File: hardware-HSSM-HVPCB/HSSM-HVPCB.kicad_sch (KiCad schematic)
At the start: 72 parts, among them J2 2601-1110, J3 Connector_BTB_20021311-00010T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, K1 G6DN-1A-L DC12, K2 G6DN-1A-L DC12, Q1 Q_NMOS_SOT-23_IRLML6344, Q2 Q_NMOS_SOT-23_IRLML6344, U1 LNK3204D-TL, U2 CS5480-INZ, U3 LTV-354T, U4 LTV-354T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

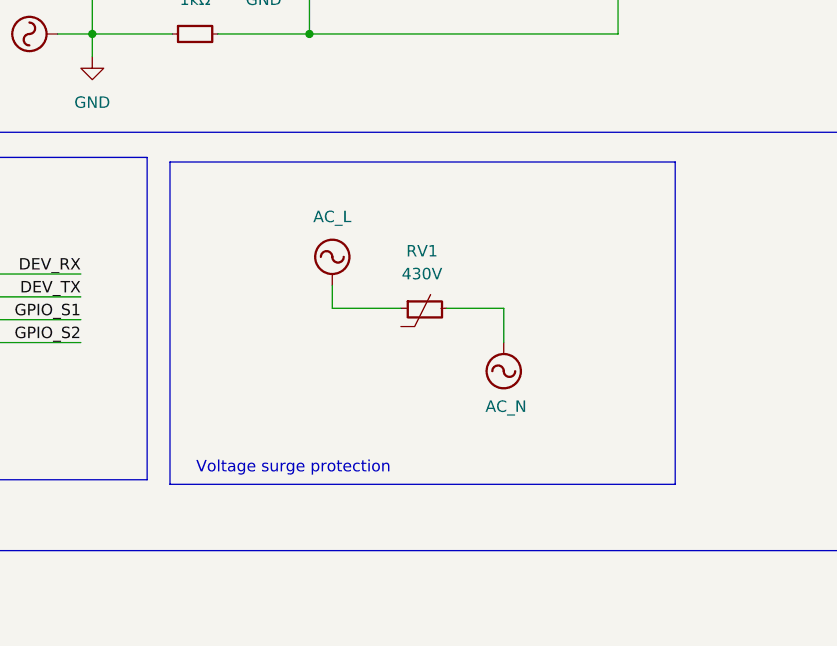
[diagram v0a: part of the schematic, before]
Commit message: [#6] Remove surge protection
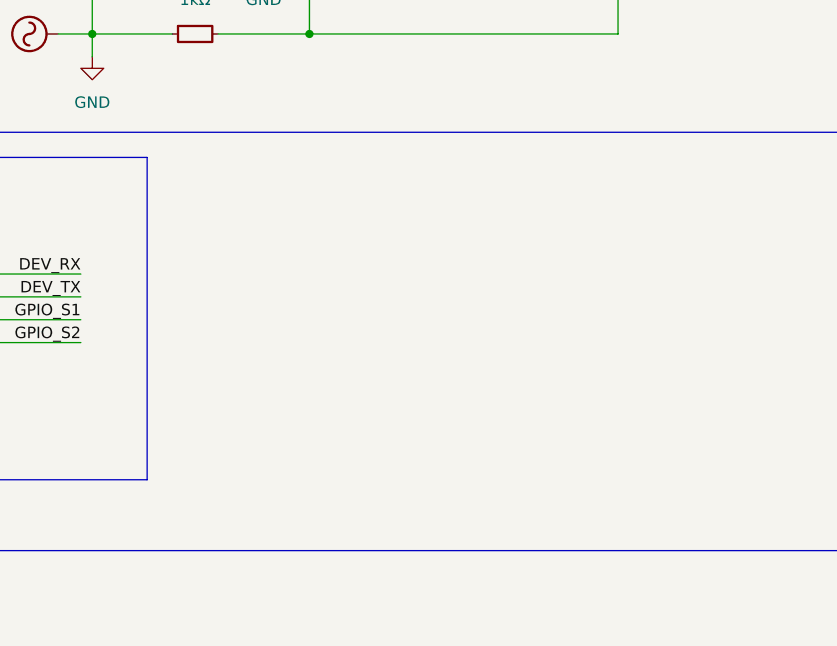
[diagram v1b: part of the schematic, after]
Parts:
- removed RV1: Varistor_MOV-14D431K, HSSM-HVPCB:MOV-14D431K, symbol HSSM-HVPCB:Varistor_MOV-14D431K
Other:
- note removed: "Voltage surge protection"

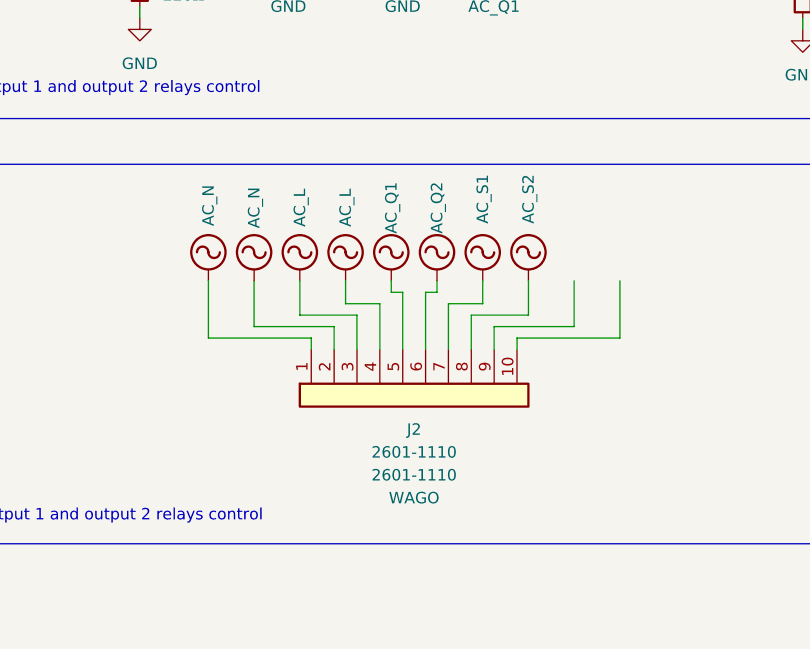
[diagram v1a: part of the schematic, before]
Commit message: [#6] Replace wago terminal with 8 pos variant
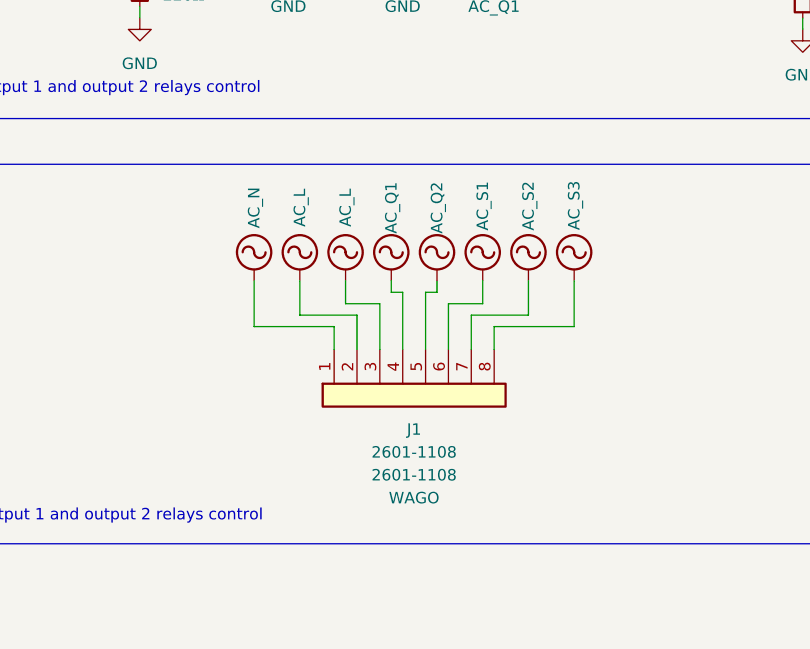
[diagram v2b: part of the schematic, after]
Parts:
- removed J2: 2601-1110, HSSM-HVPCB:2601-1110, symbol HSSM-HVPCB:terminal_1x10_2601-1110_wago
- added J1: 2601-1108, HSSM-HVPCB:2601-1108, symbol HSSM-HVPCB:terminal_1x8_2601-1108_wago
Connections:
- net AC_L: now also J1.2 (Pin_2), J1.3 (Pin_3)
- net AC_N: now also J1.1 (Pin_1)
- net AC_Q1: now also J1.4 (Pin_4)
- net AC_Q2: now also J1.5 (Pin_5)
- net AC_S1: now also J1.6 (Pin_6)
- net AC_S2: now also J1.7 (Pin_7)
- new net AC_S3: J1.8 (Pin_8)
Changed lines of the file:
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@@
 	(wire
 		(pts
-			(xy 278.13 229.87) (xy 278.13 228.6)
-		)
-		(stroke
-			(width 0)
-			(type default)
-		)
-	)
-	(wire
-		(pts
 			(xy 381 63.5) (xy 381 71.12)
 		)
@@
 	(wire
 		(pts
-			(xy 300.99 229.87) (xy 300.99 228.6)
-		)
-		(stroke
-			(width 0)
-			(type default)
-		)
-	)
-	(wire
-		(pts
 			(xy 386.08 71.12) (xy 386.08 73.66)
 		)
@@
 	(wire
 		(pts
-			(xy 266.7 228.6) (xy 266.7 222.25)
-		)
-		(stroke
-			(width 0)
-			(type default)
-		)
-	)
-	(wire
-		(pts
 			(xy 289.56 59.69) (xy 294.64 59.69)
 		)
@@
 	(wire
 		(pts
-			(xy 278.13 228.6) (xy 266.7 228.6)
-		)
-		(stroke
-			(width 0)
-			(type default)
-		)
-	)
-	(wire
-		(pts
 			(xy 354.33 46.99) (xy 354.33 52.07)
 		)
@@
 	(wire
 		(pts
-			(xy 312.42 228.6) (xy 312.42 222.25)
-		)
-		(stroke
-			(width 0)
-			(type default)
-		)
-	)
-	(wire
-		(pts
-			(xy 300.99 228.6) (xy 312.42 228.6)
-		)
-		(stroke
-			(width 0)
-			(type default)
-		)
-	)
-	(wire
-		(pts
 			(xy 350.52 185.42) (xy 350.52 187.96)
 		)
@@
 	)
 	(symbol
+		(lib_id "power:AC")
+		(at 307.34 222.25 0)
+		(unit 1)
+		(exclude_from_sim no)
+		(in_bom yes)
+		(on_board yes)
+		(dnp no)
+		(property "Reference" "#PWR030"
+			(at 307.34 224.79 0)
+			(effects
+				(font
+					(size 1.27 1.27)
+				)
+				(hide yes)
+			)
+		)
+		(property "Value" "AC_S3"
+			(at 307.34 213.868 90)
+			(effects
+				(font
+					(size 1.27 1.27)
+				)
+			)
+		)
+		(property "Footprint" ""
+			(at 307.34 222.25 0)
+			(effects
+				(font
+					(size 1.27 1.27)
+				)
+				(hide yes)
+			)
+		)
+		(property "Datasheet" ""
+			(at 307.34 222.25 0)
+			(effects
+				(font
+					(size 1.27 1.27)
+				)
+				(hide yes)
+			)
+		)
+		(property "Description" "Power symbol creates a global label with name \"AC\""
+			(at 307.34 222.25 0)
+			(effects
+				(font
+					(size 1.27 1.27)
+				)
+				(hide yes)
+			)
+		)
+		(pin "1"
+		)
+		(instances
+			(project "HSSM-HVPCB"
+				(path "/e1056638-7c6b-48e4-9e2e-c0f7b783eee5"
+					(reference "#PWR030")
+					(unit 1)
+				)
+			)
+		)
+	)
+	(symbol
 		(lib_id "HSSM-HVPCB:TPS560200DBVR_SOIC_6_TI")
 		(at 124.46 237.49 180)
@@
 	)
 	(symbol
-		(lib_id "power:AC")
-		(at 101.6 64.77 0)
-		(unit 1)
-		(exclude_from_sim no)
-		(in_bom yes)
-		(on_board yes)
-		(dnp no)
-		(property "Reference" "#PWR041"
-			(at 101.6 67.31 0)
-			(effects
-				(font
-					(size 1.27 1.27)
-				)
-				(hide yes)
-			)
-		)
-		(property "Value" "AC_L"
-			(at 101.6 58.166 0)
-			(effects
-				(font
-					(size 1.27 1.27)
-				)
-			)
-		)
-		(property "Footprint" ""
-			(at 101.6 64.77 0)
-			(effects
-				(font
-					(size 1.27 1.27)
-				)
-				(hide yes)
-			)
-		)
-		(property "Datasheet" ""
-			(at 101.6 64.77 0)
-			(effects
-				(font
-					(size 1.27 1.27)
-				)
-				(hide yes)
-			)
-		)
-		(property "Description" "Power symbol creates a global label with name \"AC\""
-			(at 101.6 64.77 0)
-			(effects
-				(font
-					(size 1.27 1.27)
-				)
-				(hide yes)
-			)
-		)
-		(pin "1"
-		)
-		(instances
-			(project "HSSM-HVPCB"
-				(path "/e1056638-7c6b-48e4-9e2e-c0f7b783eee5"
-					(reference "#PWR041")
-					(unit 1)
-				)
-			)
-		)
-	)
-	(symbol
-		(lib_id "HSSM-HVPCB:terminal_1x10_2601-1110_wago")
-		(at 288.29 234.95 90)
+		(lib_id "HSSM-HVPCB:terminal_1x8_2601-1108_wago")
+		(at 289.56 234.95 90)
 		(mirror x)
 		(unit 1)
@@
 		(on_board yes)
 		(dnp no)
-		(property "Reference" "J2"
+		(property "Reference" "J1"
 			(at 289.56 238.76 90)
 			(effects
@@
 			)
 		)
-		(property "Value" "2601-1110"
+		(property "Value" "2601-1108"
 			(at 289.56 241.3 90)
 			(effects
@@
 			)
 		)
-		(property "Footprint" "HSSM-HVPCB:2601-1110"
-			(at 288.29 234.95 0)
+		(property "Footprint" "HSSM-HVPCB:2601-1108"
+			(at 290.83 234.95 0)
 			(effects
 				(font
@@
 			)
 		)
-		(property "Datasheet" "https://www.farnell.com/datasheets/3775116.pdf"
-			(at 288.29 234.95 0)
+		(property "Datasheet" "https://source.z2data.com/2022/11/30/3/26/12/266816/8679706/WAGO26011108enUS.pdf"
+			(at 290.83 234.95 0)
 			(effects
 				(font
@@
 			)
 		)
-		(property "Description" "terminal_1x10_2601-1110_wago"
-			(at 288.29 234.95 0)
+		(property "Description" "terminal_1x10_2601-1108_wago"
+			(at 290.83 234.95 0)
 			(effects
 				(font
@@
 			)
 		)
-		(property "MPN" "2601-1110"
+		(property "MPN" "2601-1108"
 			(at 289.56 243.84 90)
 			(effects
@@
 			)
 		)
-		(pin "10"
+		(pin "3"
 		)
 		(pin "2"
 		)
-		(pin "3"
-		)
 		(pin "1"
 		)
+		(pin "7"
+		)
 		(pin "4"
 		)
@@
 		(pin "6"
 		)
-		(pin "7"
-		)
 		(pin "8"
 		)
-		(pin "9"
-		)
 		(instances
-			(project "HSSM-HVPCB"
+			(project ""
 				(path "/e1056638-7c6b-48e4-9e2e-c0f7b783eee5"
-					(reference "J2")
+					(reference "J1")
 					(unit 1)
 				)
@@
 	(symbol
 		(lib_id "power:AC")
-		(at 266.7 222.25 0)
+		(at 101.6 64.77 0)
 		(unit 1)
 		(exclude_from_sim no)
@@
 		(on_board yes)
 		(dnp no)
-		(property "Reference" "#PWR040"
-			(at 266.7 224.79 0)
+		(property "Reference" "#PWR041"
+			(at 101.6 67.31 0)
 			(effects
 				(font
@@
 			)
 		)
-		(property "Value" "AC_N"
-			(at 266.7 213.868 90)
+		(property "Value" "AC_L"
+			(at 101.6 58.166 0)
 			(effects
 				(font
@@
 		)
 		(property "Footprint" ""
-			(at 266.7 222.25 0)
+			(at 101.6 64.77 0)
 			(effects
 				(font
@@
 		)
 		(property "Datasheet" ""
-			(at 266.7 222.25 0)
+			(at 101.6 64.77 0)
 			(effects
 				(font
@@
 		)
 		(property "Description" "Power symbol creates a global label with name \"AC\""
-			(at 266.7 222.25 0)
+			(at 101.6 64.77 0)
 			(effects
 				(font
@@
 			(project "HSSM-HVPCB"
 				(path "/e1056638-7c6b-48e4-9e2e-c0f7b783eee5"
-					(reference "#PWR040")
+					(reference "#PWR041")
 					(unit 1)
 				)
@@
 		(on_board yes)
 		(dnp no)
-		(fields_autoplaced yes)
 		(property "Reference" "#PWR029"
 			(at 302.26 224.79 0)
@@
 		)
 		(property "Value" "AC_S2"
-			(at 302.2601 215.9 90)
+			(at 302.26 216.662 90)
 			(effects
 				(font
@@
 		(on_board yes)
 		(dnp no)
-		(fields_autoplaced yes)
 		(property "Reference" "#PWR028"
 			(at 297.18 224.79 0)
@@
 		)
 		(property "Value" "AC_S1"
-			(at 297.1801 215.9 90)
+			(at 297.18 216.662 90)
 			(effects
 				(font

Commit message: [#6] Replace crystal oscillator
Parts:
- removed X1: X_4.096MHz_ABLS2-4.096MHZ-D4Y-T, HSSM-HVPCB:X_HC49US, symbol HSSM-HVPCB:X_4.096MHz_ABLS2-4.096MHZ-D4Y-T
- added Y1: OSC_2520_4.096MHz_25ppm_ECS-2520MVLC-041-BN-TR, HSSM-HVPCB:ECS-2520MVLC-041-BN-TR, symbol HSSM-HVPCB:OSC_2520_4.096MHz_25ppm_ECS-2520MVLC-041-BN-TR
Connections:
- net AC_L: now also Y1.2 (GND), Y1.4 (GND)
- net at U2.1 (XIN): now also Y1.1
- net at U2.24 (XOUT): now also Y1.3
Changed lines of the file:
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@@
 	)
 	(symbol
+		(lib_id "HSSM-HVPCB:OSC_2520_4.096MHz_25ppm_ECS-2520MVLC-041-BN-TR")
+		(at 146.05 35.56 0)
+		(unit 1)
+		(exclude_from_sim no)
+		(in_bom yes)
+		(on_board yes)
+		(dnp no)
+		(fields_autoplaced yes)
+		(property "Reference" "Y1"
+			(at 146.05 24.13 0)
+			(effects
+				(font
+					(size 1.27 1.27)
+					(thickness 0.15)
+				)
+			)
+		)
+		(property "Value" "OSC_2520_4.096MHz_25ppm_ECS-2520MVLC-041-BN-TR"
+			(at 146.558 49.53 0)
+			(effects
+				(font
+					(size 1.27 1.27)
+					(thickness 0.15)
+				)
+				(justify left bottom)
+				(hide yes)
+			)
+		)
+		(property "Footprint" "HSSM-HVPCB:ECS-2520MVLC-041-BN-TR"
+			(at 146.558 52.07 0)
+			(effects
+				(font
+					(size 1.27 1.27)
+					(thickness 0.15)
+				)
+				(justify left bottom)
+				(hide yes)
+			)
+		)
+		(property "Datasheet" "https://ecsxtal.com/store/pdf/ECS-2520MVLC.pdf"
+			(at 146.558 54.61 0)
+			(effects
+				(font
+					(size 1.27 1.27)
+					(thickness 0.15)
+				)
+				(justify left bottom)
+				(hide yes)
+			)
+		)
+		(property "Description" "SMD Oscillator, 4.096 MHz, ±25 ppm, 1.6V ~ 3.6V, 2520 package"
+			(at 146.05 35.56 0)
+			(effects
+				(font
+					(size 1.27 1.27)
+				)
+				(hide yes)
+			)
+		)
+		(property "MPN" "ECS-2520MVLC-041-BN-TR"
+			(at 146.558 57.15 0)
+			(effects
+				(font
+					(size 1.27 1.27)
+					(thickness 0.15)
+				)
+				(justify left bottom)
+				(hide yes)
+			)
+		)
+		(property "Manufacturer" "ECS Inc."
+			(at 146.558 59.69 0)
+			(effects
+				(font
+					(size 1.27 1.27)
+					(thickness 0.15)
+				)
+				(justify left bottom)
+				(hide yes)
+			)
+		)
+		(property "License" "Apache-2.0"
+			(at 146.558 62.23 0)
+			(effects
+				(font
+					(size 1.27 1.27)
+				)
+				(justify left bottom)
+				(hide yes)
+			)
+		)
+		(property "Author" "Lukasz Nowarkiewicz"
+			(at 146.558 64.77 0)
+			(effects
+				(font
+					(size 1.27 1.27)
+				)
+				(justify left bottom)
+				(hide yes)
+			)
+		)
+		(property "Val" "4.096MHz"
+			(at 146.05 26.67 0)
+			(effects
+				(font
+					(size 1.27 1.27)
+				)
+			)
+		)
+		(pin "1"
+		)
+		(pin "4"
+		)
+		(pin "3"
+		)
+		(pin "2"
+		)
+		(instances
+			(project ""
+				(path "/e1056638-7c6b-48e4-9e2e-c0f7b783eee5"
+					(reference "Y1")
+					(unit 1)
+				)
+			)
+		)
+	)
+	(symbol
 		(lib_id "power:GND")
 		(at 151.13 243.84 0)
@@
 					(unit 1)
 				)
-			)
-		)
-	)
-	(symbol
-		(lib_id "HSSM-HVPCB:X_4.096MHz_ABLS2-4.096MHZ-D4Y-T")
-		(at 146.05 35.56 0)
-		(unit 1)
-		(exclude_from_sim no)
-		(in_bom yes)
-		(on_board yes)
-		(dnp no)
-		(fields_autoplaced yes)
-		(property "Reference" "X1"
-			(at 146.05 24.13 0)
-			(effects
-				(font
-					(size 1.27 1.27)
-					(thickness 0.15)
-				)
-			)
-		)
-		(property "Value" "X_4.096MHz_ABLS2-4.096MHZ-D4Y-T"
-			(at 146.05 49.022 0)
-			(effects
-				(font
-					(size 1.27 1.27)
-					(thickness 0.15)
-				)
-				(justify left bottom)
-				(hide yes)
-			)
-		)
-		(property "Footprint" "HSSM-HVPCB:X_HC49US"
-			(at 146.05 51.562 0)
-			(effects
-				(font
-					(size 1.27 1.27)
-					(thickness 0.15)
-				)
-				(justify left bottom)
-				(hide yes)
-			)
-		)
-		(property "Datasheet" "https://abracon.com/Resonators/ABLS2.pdf"
-			(at 146.05 54.102 0)
-			(effects
-				(font
-					(size 1.27 1.27)
-					(thickness 0.15)
-				)
-				(justify left bottom)
-				(hide yes)
-			)
-		)
-		(property "Description" "Quartz Crystal, 4.096 MHz, ±30ppm, 18pF, HC-49/US, Abracon"
-			(at 146.05 35.56 0)
-			(effects
-				(font
-					(size 1.27 1.27)
-				)
-				(hide yes)
-			)
-		)
-		(property "MPN" "ABLS2-4.096MHZ-D4Y-T"
-			(at 146.05 56.642 0)
-			(effects
-				(font
-					(size 1.27 1.27)
-					(thickness 0.15)
-				)
-				(justify left bottom)
-				(hide yes)
-			)
-		)
-		(property "Manufacturer" "Abracon"
-			(at 146.05 59.182 0)
-			(effects
-				(font
-					(size 1.27 1.27)
-					(thickness 0.15)
-				)
-				(justify left bottom)
-				(hide yes)
-			)
-		)
-		(property "License" "Apache-2.0"
-			(at 146.05 61.722 0)
-			(effects
-				(font
-					(size 1.27 1.27)
-				)
-				(justify left bottom)
-				(hide yes)
-			)
-		)
-		(property "Author" "Lukasz Nowarkiewicz"
-			(at 146.05 64.262 0)
-			(effects
-				(font
-					(size 1.27 1.27)
-				)
-				(justify left bottom)
-				(hide yes)
-			)
-		)
-		(property "Val" "4.096MHz"
-			(at 146.05 26.67 0)
-			(effects
-				(font
-					(size 1.27 1.27)
-				)
-			)
-		)
-		(pin "3"
-		)
-		(pin "4"
-		)
-		(pin "2"
-		)
-		(pin "1"
-		)
-		(instances
-			(project "HSSM-HVPCB"
-				(path "/e1056638-7c6b-48e4-9e2e-c0f7b783eee5"
-					(reference "X1")
-					(unit 1)
-				)

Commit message: [#6] Remove status LEDs from HVPCB
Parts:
- removed D7, D8: LED_Green_Kingbright_APHHS1005CGCK, HSSM-HVPCB:LED_1005, symbol HSSM-HVPCB:LED_Green_Kingbright_APHHS1005CGCK
- removed R10, R9: R_220R_1pct_0402_RC0402FR-07220RL, HSSM-HVPCB:R_0402, symbol HSSM-HVPCB:R_220R_1pct_0402_RC0402FR-07220RL

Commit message: [#3] Remove fuses
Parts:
- removed F3, F4: F_4A_SlowBlow_Holder_UMZ250_3404.2422.11, HSSM-HVPCB:F_Holder_UMZ250, symbol HSSM-HVPCB:F_4A_SlowBlow_Holder_UMZ250_3404.2422.11
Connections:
- net AC_Q1: now also K1.5
- net AC_Q2: now also K2.5

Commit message: [#7] Placement WIP
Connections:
- net AC_L: now also J1.4 (Pin_4), J1.5 (Pin_5); no longer J1.2 (Pin_2), J1.3 (Pin_3)
- net AC_N: now also J1.3 (Pin_3); no longer J1.1 (Pin_1)
- net AC_Q1: now also J1.1 (Pin_1); no longer J1.4 (Pin_4)
- net AC_Q2: now also J1.8 (Pin_8); no longer J1.5 (Pin_5)
- net AC_S1: now also J1.2 (Pin_2); no longer J1.6 (Pin_6)
- net AC_S3: now also J1.6 (Pin_6); no longer J1.8 (Pin_8)
